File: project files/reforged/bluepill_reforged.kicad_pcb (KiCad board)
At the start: 2 copper layers, 53.3 x 22.9 mm, 40 parts, among them J1 USB_C_Receptacle_USB2.0, J2 Left Castellation, J3 STDC14, J4 Right Castellation, SW1 Boot0, SW2 Reset, U1 AMS1117-3.3, U2 STM32F103C8Tx, Y1 8Mhz,TSX-3225, Y2 MC-306, 32768Hz

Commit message: rearranged
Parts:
- added J5: STDC14, Connector_PinHeader_1.27mm:PinHeader_2x07_P1.27mm_Vertical, F.Cu at (174.6, 134.6)
- C13, C14: moved to F.Cu
- R9: moved to B.Cu
- Y1: value 8Mhz,TSX-3225 -> 8MHz; footprint Crystal:Crystal_SMD_3225-4Pin_3.2x2.5mm -> Crystal:Crystal_SMD_TXC_7M-4Pin_3.2x2.5mm
- moved R11 33.9 mm to (137.7, 143.5), turned to 0 degrees
- moved D3 33.1 mm to (137.2, 142.7), turned to 0 degrees
- moved C13 27.3 mm to (176.8, 143.8)
- moved C9 18.5 mm to (158.4, 138.4)
- moved C3 12.9 mm to (154.3, 138.4)
- moved R4 11.9 mm to (154.3, 140.3)
- moved F1 10.7 mm to (121.9, 139.2), turned to 90 degrees
- moved C1 10.6 mm to (142.2, 142.9)
- moved C2 10.6 mm to (142.2, 134.0)
- moved R5 9.49 mm to (150.5, 138.4), turned to 90 degrees
- moved D4 8.95 mm to (177.8, 142.9)
- moved C11 7.77 mm to (154.1, 142.9)
- moved C14 7.69 mm to (137.2, 133.6)
- moved C12 6.75 mm to (154.1, 136.5), turned to 0 degrees
- moved R7 6.35 mm to (137.2, 135.1)
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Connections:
- J1 pad A8: Net-(J1-PadA8) -> (no net)
- J1 pad B8: Net-(J1-PadB8) -> (no net)
- J3 pad 1: Net-(J3-Pad1) -> (no net)
- J3 pad 10: Net-(J3-Pad10) -> (no net)
- J3 pad 2: Net-(J3-Pad2) -> (no net)
- J3 pad 9: Net-(J3-Pad9) -> (no net)
- Y2 pad 2: Net-(Y2-Pad2) -> (no net)
- Y2 pad 3: Net-(Y2-Pad3) -> (no net)
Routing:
- net PB1: track 0.00 -> 7.78 mm
- net PB0: track 0.00 -> 5.98 mm
- net D-: track 5.41 -> 0.00 mm
- net D+: track 5.41 -> 0.00 mm
- net PA7: track 0.00 -> 4.72 mm
- net PA12: track 4.35 -> 0.00 mm
- net Net-(J1-PadA5): track 3.58 -> 0.00 mm
- net VBUS: track 2.73 -> 0.00 mm
- net Net-(J1-PadB5): track 2.55 -> 0.00 mm
- net OSCOUT: vias 1 -> 0
- net OSCIN: vias 1 -> 0
- net NRST: vias 1 -> 0
- net BOOT1: vias 1 -> 0
- net +3V3: vias 3 -> 0
- added copper zone on B.Cu, net GNDD
- added copper zone on F.Cu, net GNDD
- removed copper zone on B.Cu, net GNDREF
- removed copper zone on F.Cu, net GNDREF
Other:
- net class Default: via_dia 0.8 -> 0.5; via_drill 0.4 -> 0.3
- board text removed: "+3.3"
- board text removed: "A0"
- board text removed: "A1"
- board text removed: "A10"
- board text removed: "A11"
- board text removed: "A12"
- board text removed: "A15"
- board text removed: "A2"
- board text removed: "A3"
- board text removed: "A4"
- board text removed: "A5"
- board text removed: "A6"
- board text removed: "A7"
- board text removed: "A8"
- board text removed: "A9"
- board text removed: "B0"
- board text removed: "B1"
- board text removed: "B10"
- board text removed: "B11"
- board text removed: "B12"
- board text removed: "B13"
- board text removed: "B14"
- board text removed: "B15"
- board text removed: "B3"
- board text removed: "B4"
- board text removed: "B5"
- board text removed: "B6"
- board text removed: "B7"
- board text removed: "B8"
- board text removed: "B9"
- board text removed: "BAT"
- board text removed: "C13"
- board text removed: "C14"
- board text removed: "C15"
- board text removed: "G"
- board text removed: "Vin"
- board text removed: "~R"

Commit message: edits
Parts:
- R10: moved to F.Cu
- moved D4 40.7 mm to (144.1, 120.0)
- moved C13 34.2 mm to (151.4, 120.9)
- moved C2 34.2 mm to (116.8, 111.1)
- moved C3 34.2 mm to (128.9, 115.6)
- moved F1 34.2 mm to (96.5, 116.3)
- moved J1 34.2 mm to (105.9, 115.6)
- moved J2 34.2 mm to (152.4, 123.2)
- moved R4 34.2 mm to (128.9, 117.5)
- moved R5 34.2 mm to (125.1, 115.6)
- moved R9 34.2 mm to (112.3, 110.0)
- moved Y1 34.2 mm to (138.4, 111.1)
- moved Y2 34.2 mm to (138.4, 117.5)
- moved C1 34.2 mm to (116.8, 120.0)
- moved C11 34.2 mm to (128.7, 120.0)
- moved C12 34.2 mm to (128.7, 113.7)
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
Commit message: Update bluepill_reforged.kicad_pcb
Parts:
- moved SW2 1.09 mm to (116.8, 111.1)
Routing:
- net PA0: track 0.00 -> 13.7 mm, vias 0 -> 1
- net PB11: track 0.00 -> 12.3 mm
- net PA1: track 0.00 -> 11.4 mm
- net NRST: track 0.00 -> 10.2 mm
- net PB10: track 0.00 -> 9.91 mm
- net PA2: track 0.00 -> 9.02 mm, vias 0 -> 1
- net PA3: track 0.00 -> 8.57 mm, vias 0 -> 1
- net PA4: track 0.00 -> 7.91 mm
- net PA5: track 0.00 -> 6.52 mm
- net PA6: track 0.00 -> 5.04 mm

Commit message: Updates after re-opening in KiCAD 5.1.7
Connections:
- J1 pad A8: (no net) -> Net-(J1-PadA8)
- J1 pad B8: (no net) -> Net-(J1-PadB8)
- J3 pad 1: (no net) -> Net-(J3-Pad1)
- J3 pad 10: (no net) -> Net-(J3-Pad10)
- J3 pad 2: (no net) -> Net-(J3-Pad2)
- J3 pad 9: (no net) -> Net-(J3-Pad9)
- J5 pad 1: (no net) -> Net-(J5-Pad1)
- J5 pad 10: (no net) -> Net-(J5-Pad10)
- J5 pad 2: (no net) -> Net-(J5-Pad2)
- J5 pad 9: (no net) -> Net-(J5-Pad9)
- Y2 pad 2: (no net) -> Net-(Y2-Pad2)
- Y2 pad 3: (no net) -> Net-(Y2-Pad3)

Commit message: couple comments
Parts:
- removed the J3 at (149.9, 115.6)
- added J4: STDC14-THT, Connector_PinHeader_1.27mm:PinHeader_2x07_P1.27mm_Vertical, F.Cu at (150.5, 111.8)
- J5: value STDC14 -> STDC14-SMD; footprint Connector_PinHeader_1.27mm:PinHeader_2x07_P1.27mm_Vertical -> Connector_PinHeader_1.27mm:PinHeader_2x07_P1.27mm_Vertical_SMD
- moved J5 3.86 mm to (151.1, 115.6), turned to 0 degrees
- renumbered C10 to C1, C8 to C10, C14 to C11, C9 to C12, C1 to C13, C2 to C14, C11 to C2, C12 to C3, C13 to C4, C7 to C6, C3 to C7, C4 to C8, C6 to C9, J4 to J3, R10 to R1, R9 to R10, R5 to R11, R7 to R2, R1 to R3, R2 to R4, R6 to R5, R11 to R6, R3 to R7, R4 to R9, U2 to U1, U1 to U2, Y2 to Y1, Y1 to Y2

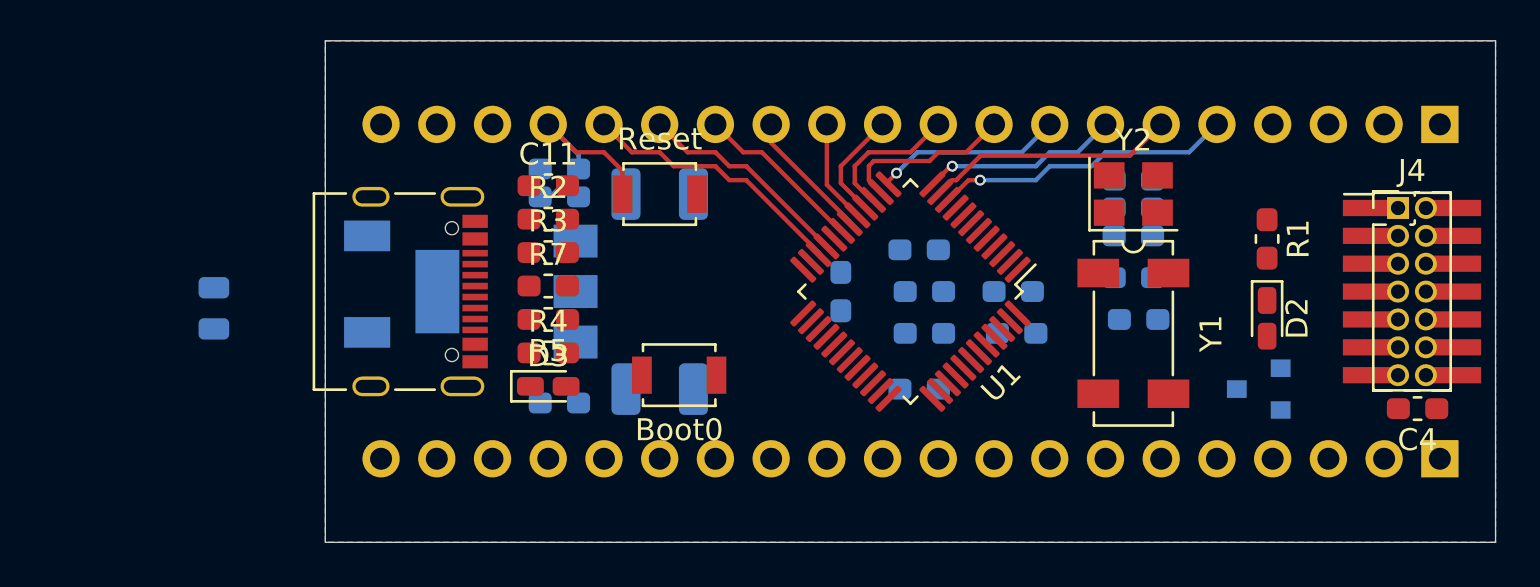
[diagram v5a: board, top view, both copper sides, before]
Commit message: Added lo-pass filter for VCCA
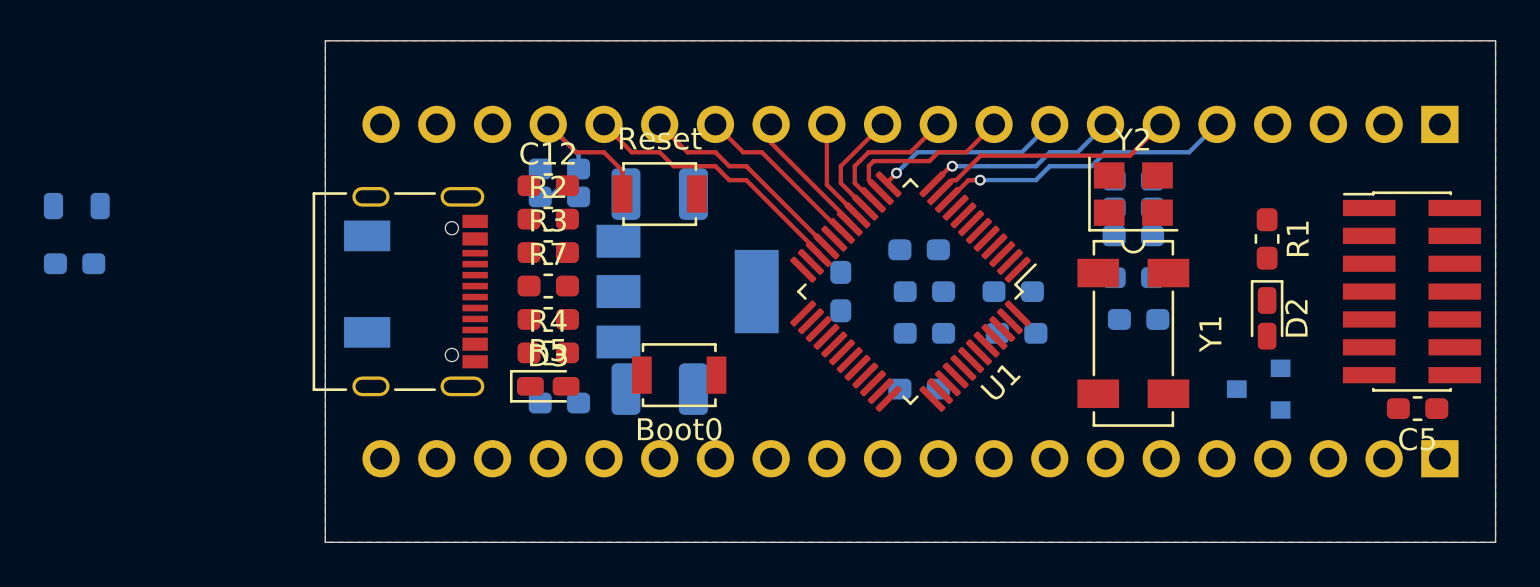
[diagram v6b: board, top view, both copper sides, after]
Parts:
- removed F1: 1A, Fuse:Fuse_0805_2012Metric
- removed the J4 at (150.5, 111.8)
- added C4: 1u, Capacitor_SMD:C_0603_1608Metric_Pad1.05x0.95mm_HandSolder, B.Cu at (90.2, 114.3)
- added FB1: Ferrite_Bead, Inductor_SMD:L_0805_2012Metric, B.Cu at (90.3, 111.7)
- C14: renamed from C13; value 0.1-10 uF -> 10 uF
- C15: renamed from C14; value 47-1000 uF -> 100 uF
- D1: value 1A -> 0.5A
- U2: value AMS1117-3.3 -> LD1117S33
- moved U2 8.25 mm to (118.1, 115.6), turned to 0 degrees
- renumbered C9 to C10, C10 to C11, C11 to C12, C12 to C13, C4 to C5, C5 to C6, C6 to C7, C7 to C8, C8 to C9, J5 to J4
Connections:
- C5 pad 1: +3V3 -> +3.3VA
- D1 pad 2: Net-(D1-Pad2) -> VBUS
- U1 pad 9: +3V3 -> +3.3VA

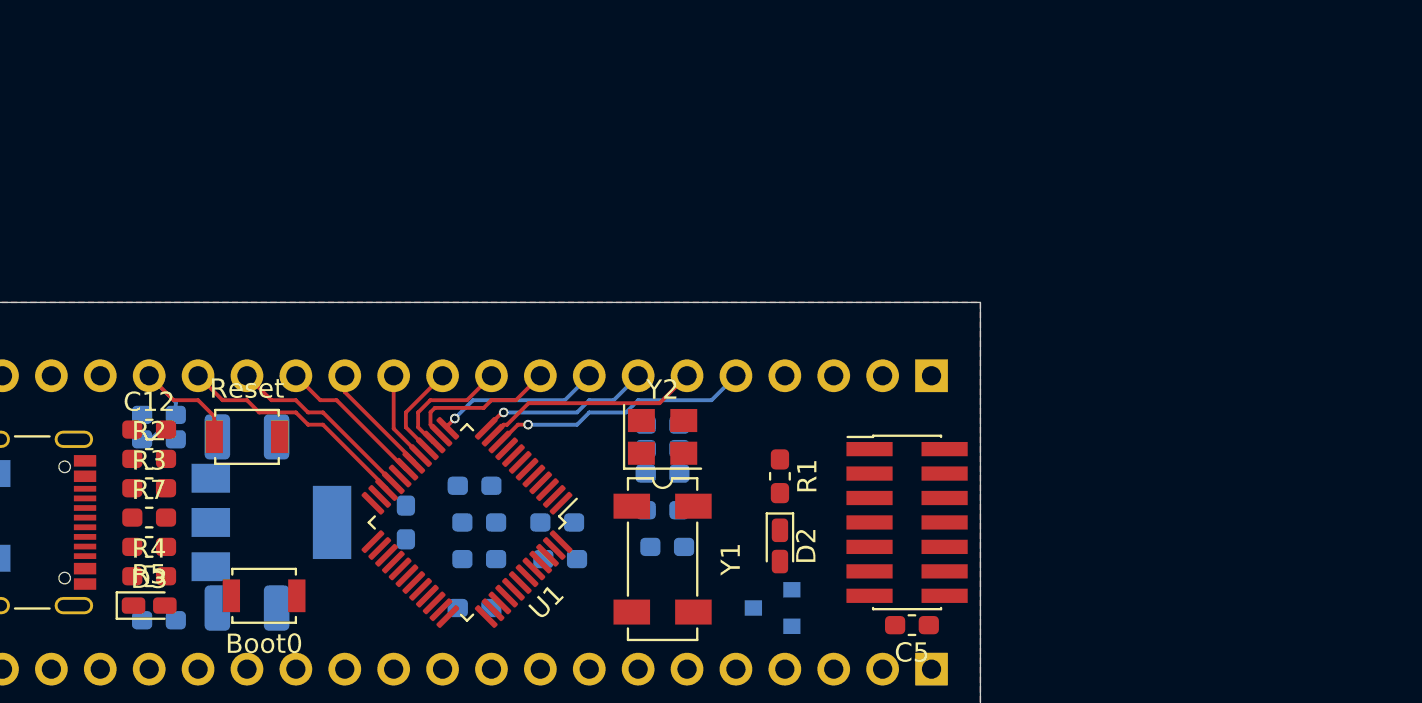
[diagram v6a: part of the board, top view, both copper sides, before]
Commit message: Added QWIIC connector
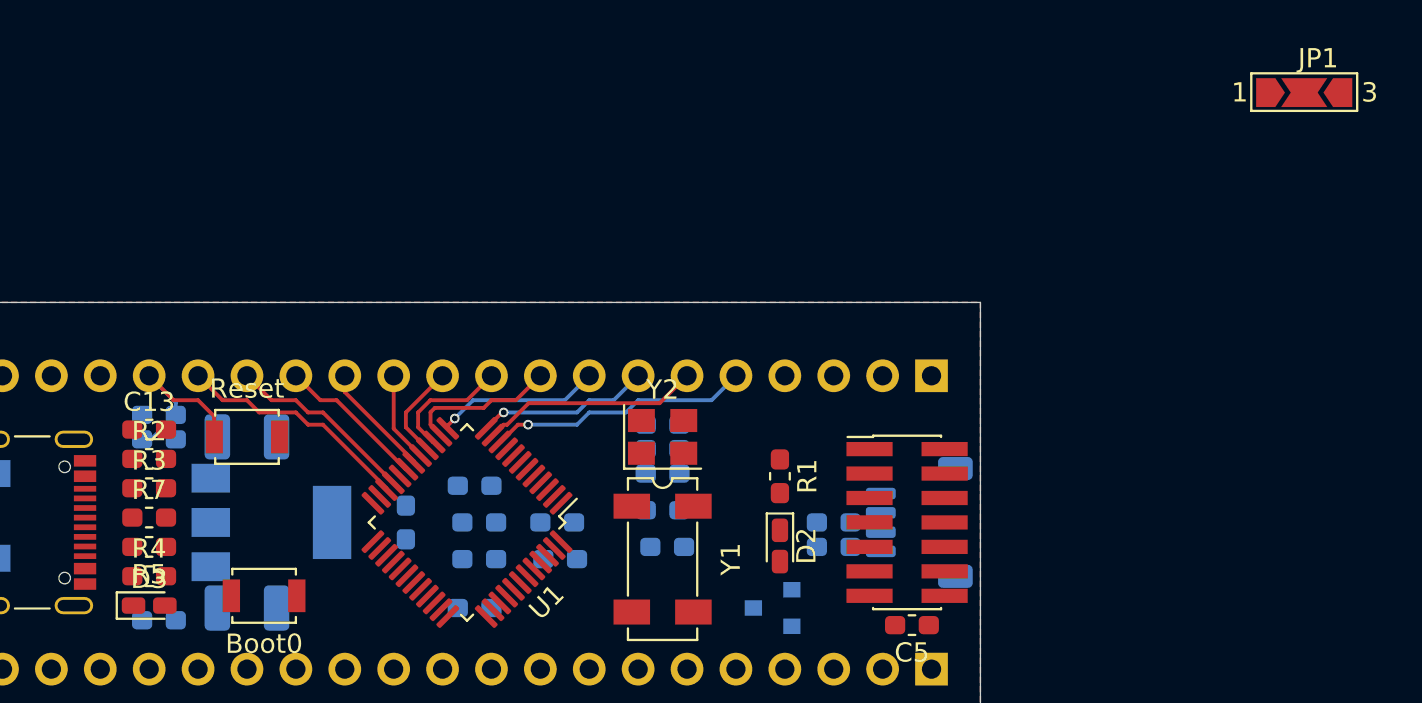
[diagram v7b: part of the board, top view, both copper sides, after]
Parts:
- added J5: Qwiik, Connector_JST:JST_SH_SM04B-SRSS-TB_1x04-1MP_P1.00mm_Horizontal, B.Cu at (151.8, 115.6)
- added JP1: I2C Pull-Up, Jumper:SolderJumper-3_P2.0mm_Open_TrianglePad1.0x1.5mm_NumberLabels, F.Cu at (171.8, 93.2)
- added R12: 2K2, Resistor_SMD:R_0603_1608Metric_Pad1.05x0.95mm_HandSolder, B.Cu at (147.3, 116.8)
- added R13: 2K2, Resistor_SMD:R_0603_1608Metric_Pad1.05x0.95mm_HandSolder, B.Cu at (147.3, 115.6)
- renumbered C13 to C12, C12 to C13, J4 to J2, J2 to J3, J3 to J4

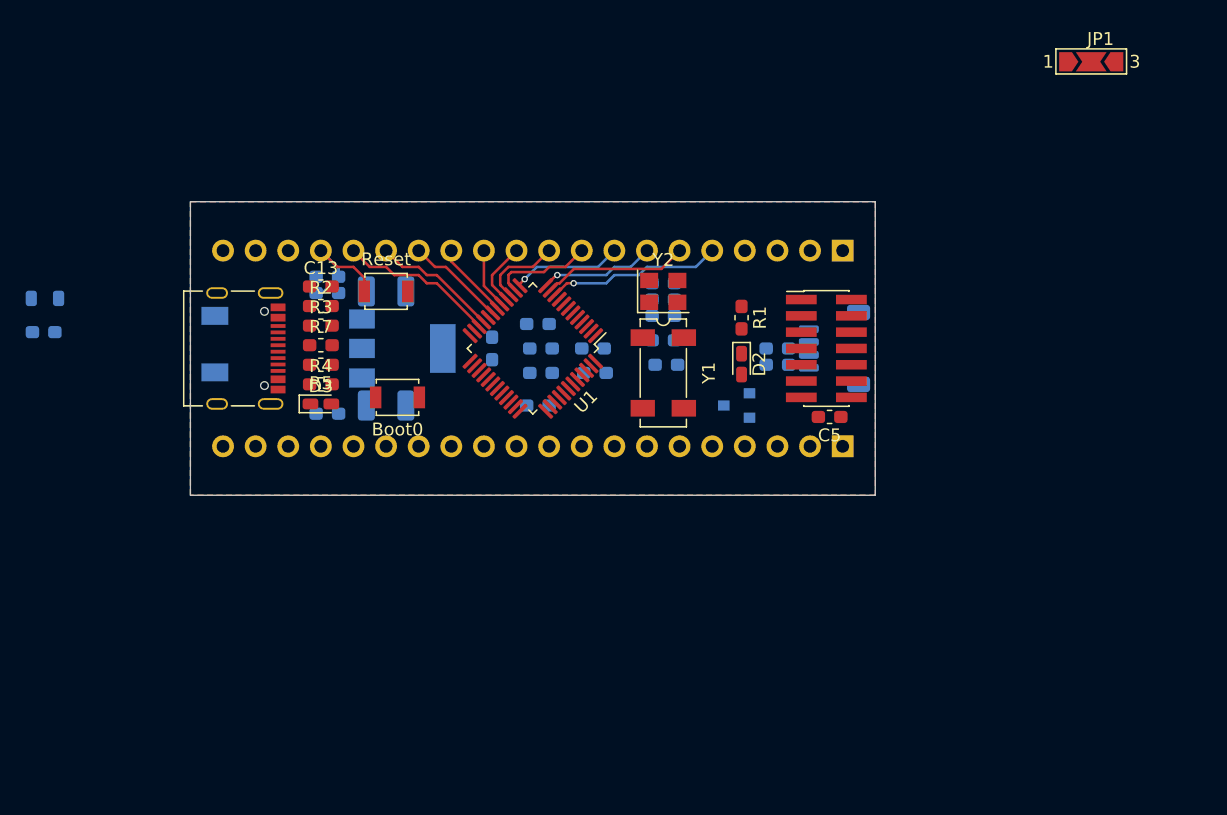
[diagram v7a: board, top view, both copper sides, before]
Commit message: push when github lagged
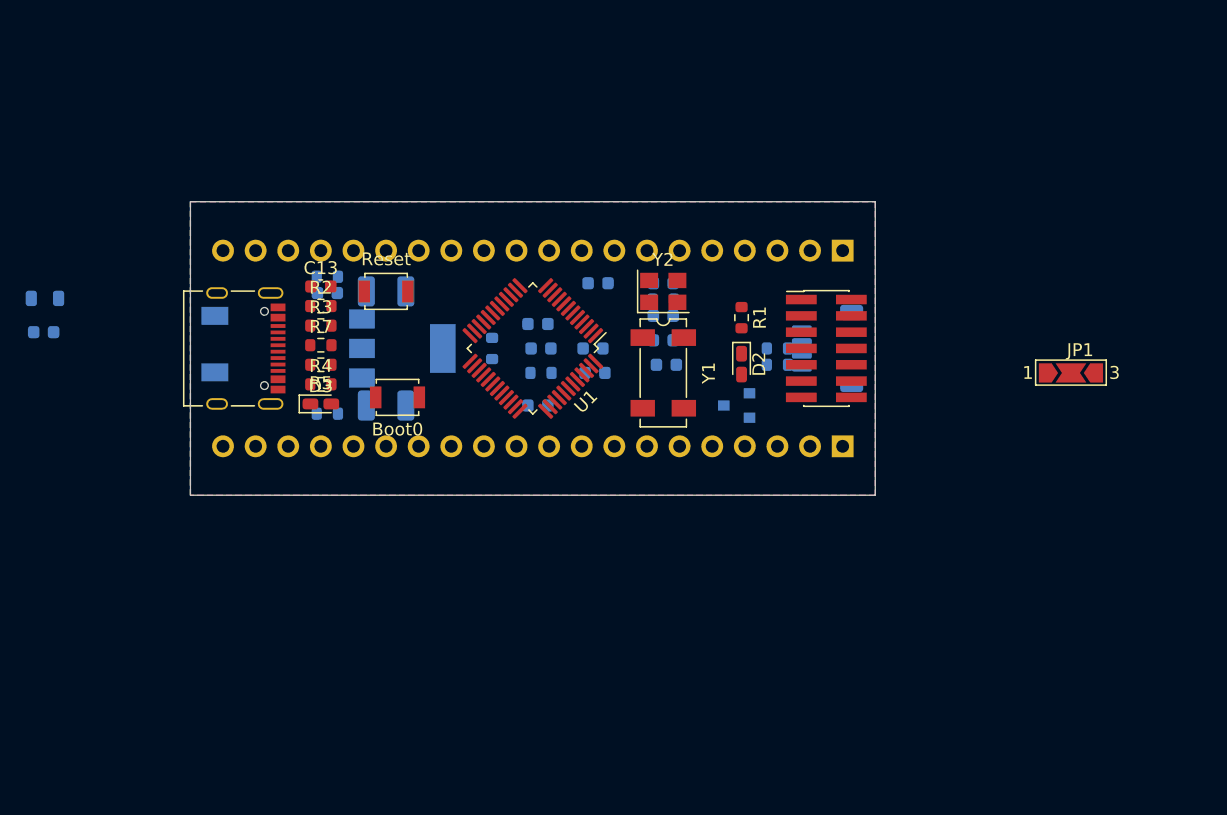
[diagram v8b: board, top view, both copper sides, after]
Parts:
- C1, C10, C11, C12, C13, C2, C3, C4, C6, C7, C8, C9: footprint Capacitor_SMD:C_0603_1608Metric_Pad1.05x0.95mm_HandSolder -> Capacitor_SMD:C_0603_1608Metric
- C5: footprint Capacitor_SMD:C_0603_1608Metric_Pad1.05x0.95mm_HandSolder -> Capacitor_SMD:C_0603_1608Metric; moved to B.Cu
- J2: value STDC14-SMD -> STDC14
- R1, R10, R11, R12, R13, R2, R3, R4, R5, R6, R7, R8, R9: footprint Resistor_SMD:R_0603_1608Metric_Pad1.05x0.95mm_HandSolder -> Resistor_SMD:R_0603_1608Metric
- moved JP1 24.3 mm to (170.2, 117.5)
- moved C5 20.8 mm to (133.3, 110.5), turned to 0 degrees
- moved J5 0.54 mm to (151.2, 115.6)
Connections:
- J2 pad 13: PA10 -> PA9
- J2 pad 14: PA9 -> PA10
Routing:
- net PA0: track 13.7 -> 0.00 mm, vias 1 -> 0
- net PB11: track 12.3 -> 0.00 mm
- net PA1: track 11.4 -> 0.00 mm
- net NRST: track 10.2 -> 0.00 mm
- net PB10: track 9.91 -> 0.00 mm
- net PA2: track 9.02 -> 0.00 mm, vias 1 -> 0
- net PA3: track 8.57 -> 0.00 mm, vias 1 -> 0
- net PA4: track 7.91 -> 0.00 mm
- net PB1: track 7.78 -> 0.00 mm
- net PA5: track 6.52 -> 0.00 mm
- net PB0: track 5.98 -> 0.00 mm
- net PA6: track 5.04 -> 0.00 mm
- net PA7: track 4.72 -> 0.00 mm
